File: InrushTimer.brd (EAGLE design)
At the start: 62.2 x 36 mm, 71 parts, among them IC1 TLC272D, IC2 555, IC3 4076N, Q2 TRANSISTOR-FET_2N7002, Q3 TRANSISTOR-FET_2N7002, Q4 TRANSISTOR-FET_2N7002, Q5 TRANSISTOR-FET_2N7002, Q6 DIODES_ZTX451DIODES_ZTX451_0_0, T1 MMBTA05, U1 ROHM_BY_ELEMENT14_BATCH_1_BU4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

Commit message: Layout changes.
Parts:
- moved C5 1.62 mm to (5.71, 31.4), turned to 180 degrees
- moved D4 0.32 mm to (2.06, 29.8)
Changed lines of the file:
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@@
 <setting verticaltext="up"/>
 </settings>
-<grid distance="0.05" unitdist="inch" unit="inch" style="lines" multiple="1" display="yes" altdistance="0.00625" altunitdist="inch" altunit="inch"/>
+<grid distance="0.05" unitdist="inch" unit="inch" style="lines" multiple="1" display="yes" altdistance="0.0125" altunitdist="inch" altunit="inch"/>
 <layers>
 <layer number="1" name="Top" color="4" fill="1" visible="yes" active="yes"/>
@@
 <element name="R3" library="rcl" package="0207/2V" value="10K" x="18.0975" y="9.8425" rot="R225"/>
 <element name="C10" library="rcl" package="C0805K" value="10pF (DNF)" x="73.025" y="27.305" rot="MR180"/>
-<element name="D4" library="diode" package="DO41-7.6" value="STTH110" x="2.06375" y="30.1625" rot="R270"/>
+<element name="D4" library="diode" package="DO41-7.6" value="STTH110" x="2.06375" y="29.845" rot="R270"/>
 <element name="IC1" library="linear" package="SO08" value="TLC272D" x="12.3825" y="25.4" smashed="yes" rot="MR0">
 <attribute name="NAME" x="15.0495" y="23.495" size="1.27" layer="26" rot="MR90"/>
@@
 <attribute name="MF" value="" x="56.515" y="30.7975" size="1.778" layer="27" rot="R90" display="off"/>
 </element>
-<element name="C5" library="rcl" package="C0805K" value="10nF" x="4.1275" y="31.75" rot="MR0"/>
+<element name="C5" library="rcl" package="C0805K" value="10nF" x="5.715" y="31.4325" rot="MR180"/>
 <element name="C4" library="rcl" package="C050-024X044" value="10nF" x="20.6375" y="8.255" rot="R45"/>
 <element name="C6" library="rcl" package="C0805K" value="1nF" x="18.0975" y="25.4" rot="MR90"/>
@@
 <wire x1="70.00875" y1="18.415" x2="72.920721875" y2="17.090525" width="0" layer="19" extent="1-1"/>
 <wire x1="45.24375" y1="1.74625" x2="70.00875" y2="8.255" width="0" layer="19" extent="1-1"/>
-<wire x1="41.165" y1="12.065" x2="45.24375" y2="1.74625" width="0" layer="19" extent="16-16"/>
-<wire x1="38.735" y1="9.525" x2="41.165" y2="12.065" width="0" layer="19" extent="16-16"/>
+<wire x1="38.735" y1="9.525" x2="45.24375" y2="1.74625" width="0" layer="19" extent="1-1"/>
+<wire x1="41.165" y1="12.065" x2="38.735" y2="9.525" width="0" layer="19" extent="16-16"/>
 <wire x1="32.86125" y1="16.98625" x2="38.735" y2="9.525" width="0" layer="19" extent="1-1"/>
 <wire x1="24.710525" y1="9.153025" x2="32.86125" y2="16.98625" width="0" layer="19" extent="1-1"/>
@@
 <wire x1="15.5575" y1="5.08" x2="15.5575" y2="5.395" width="0.4064" layer="16"/>
 <wire x1="17.2593" y1="3.7973" x2="17.2593" y2="5.08" width="0.4064" layer="16"/>
-<wire x1="5.1275" y1="31.75" x2="5.715" y2="31.1625" width="0.6096" layer="16"/>
-<wire x1="5.715" y1="31.1625" x2="5.715" y2="28.8925" width="0.6096" layer="16"/>
 <wire x1="5.715" y1="28.8925" x2="8.5725" y2="28.8925" width="0.6096" layer="16"/>
 <wire x1="18.995525" y1="10.740525" x2="19.25855" y2="10.4775" width="0.6096" layer="16"/>
@@
 <wire x1="10.00125" y1="22.86" x2="10.00125" y2="14.976971875" width="0.6096" layer="16"/>
 <wire x1="10.00125" y1="14.976971875" x2="10.531971875" y2="14.976971875" width="0.6096" layer="16"/>
+<wire x1="5.715" y1="28.8925" x2="5.6675" y2="28.8925" width="0.6096" layer="16"/>
+<wire x1="5.715" y1="28.8925" x2="4.715" y2="29.8925" width="0.6096" layer="16"/>
+<wire x1="4.715" y1="29.8925" x2="4.715" y2="31.4325" width="0.6096" layer="16"/>
 <wire x1="83.65" y1="32.7" x2="81.11" y2="35.24" width="0" layer="19" extent="1-1"/>
 <wire x1="77.62875" y1="26.035" x2="83.65" y2="32.7" width="0" layer="19" extent="1-1"/>
@@
 <wire x1="45.24375" y1="6.82625" x2="45.87875" y2="9.04875" width="0" layer="19" extent="1-1"/>
 <wire x1="33.765" y1="12.065" x2="42.79125" y2="14.12875" width="0" layer="19" extent="16-16"/>
+<wire x1="32.385" y1="14.605" x2="33.765" y2="12.065" width="0" layer="19" extent="16-16"/>
 <wire x1="34.501434375" y1="6.84706875" x2="33.765" y2="12.065" width="0" layer="19" extent="16-16"/>
 <wire x1="30.7975" y1="3.81" x2="34.501434375" y2="6.84706875" width="0" layer="19" extent="16-16"/>
 <wire x1="19.25855" y1="10.4775" x2="18.415" y2="5.08" width="0" layer="19" extent="16-16"/>
-<wire x1="32.385" y1="14.605" x2="33.765" y2="12.065" width="0" layer="19" extent="16-16"/>
 <wire x1="12.065" y1="11.43" x2="15.5575" y2="5.395" width="0" layer="19" extent="16-16"/>
 <wire x1="15.594253125" y1="32.42175" x2="8.73125" y2="28.73375" width="0" layer="19" extent="16-16"/>
@@
 <contactref element="IC1" pad="5"/>
 <contactref element="R8" pad="2"/>
-<wire x1="2.06375" y1="33.9725" x2="2.8575" y2="33.9725" width="0.6096" layer="16"/>
-<wire x1="2.8575" y1="33.9725" x2="5.715" y2="33.9725" width="0.6096" layer="16"/>
-<wire x1="3.1275" y1="31.75" x2="2.8575" y2="32.02" width="0.6096" layer="16"/>
-<wire x1="2.8575" y1="32.02" x2="2.8575" y2="33.9725" width="0.6096" layer="16"/>
+<wire x1="2.06375" y1="33.9725" x2="5.715" y2="33.9725" width="0.6096" layer="16"/>
 <wire x1="5.715" y1="33.9725" x2="8.255" y2="33.9725" width="0.6096" layer="16"/>
 <wire x1="8.5725" y1="31.4325" x2="8.5725" y2="33.9725" width="0.6096" layer="16"/>
@@
 <wire x1="8.89" y1="31.4325" x2="8.5725" y2="31.4325" width="0.4064" layer="16"/>
 <wire x1="10.4775" y1="28" x2="10.4775" y2="29.845" width="0.4064" layer="16"/>
+<wire x1="2.06375" y1="33.9725" x2="2.06375" y2="33.655" width="0.6096" layer="16"/>
+<wire x1="8.5725" y1="31.4325" x2="6.715" y2="31.4325" width="0.6096" layer="16"/>
 </signal>
 <signal name="N$7">
@@
 <wire x1="41.165" y1="14.605" x2="45.79125" y2="14.12875" width="0" layer="19" extent="16-16"/>
 <wire x1="41.165" y1="13.335" x2="41.165" y2="14.605" width="0" layer="19" extent="16-16"/>
-<wire x1="35.2425" y1="26.035" x2="45.79125" y2="14.12875" width="0" layer="19" extent="16-16"/>
+<wire x1="35.2425" y1="26.035" x2="41.165" y2="14.605" width="0" layer="19" extent="16-16"/>
 </signal>
 <signal name="ON_B">
@@
 <wire x1="4.425" y1="22.30375" x2="3.73125" y2="22.30375" width="1.4224" layer="16"/>
 <wire x1="3.73125" y1="22.30375" x2="2.06375" y2="23.97125" width="1.4224" layer="16"/>
-<wire x1="2.06375" y1="23.97125" x2="2.06375" y2="26.3525" width="1.4224" layer="16"/>
+<wire x1="2.06375" y1="23.97125" x2="2.06375" y2="26.035" width="1.4224" layer="16"/>
 </signal>
 <signal name="ON_A_SYNC">

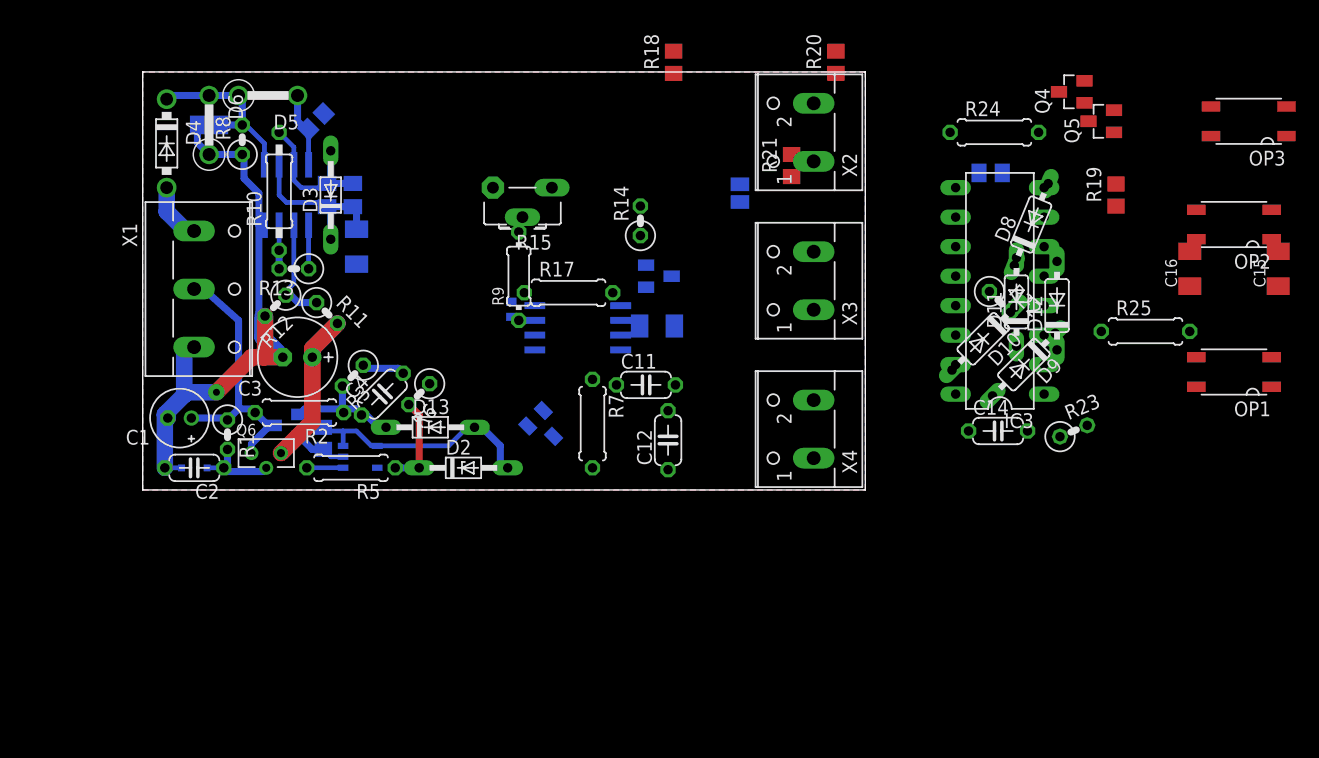
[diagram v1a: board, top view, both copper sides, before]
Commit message: ayed out the timer - starting on the D types. Fixed incorrect gate capacitance.
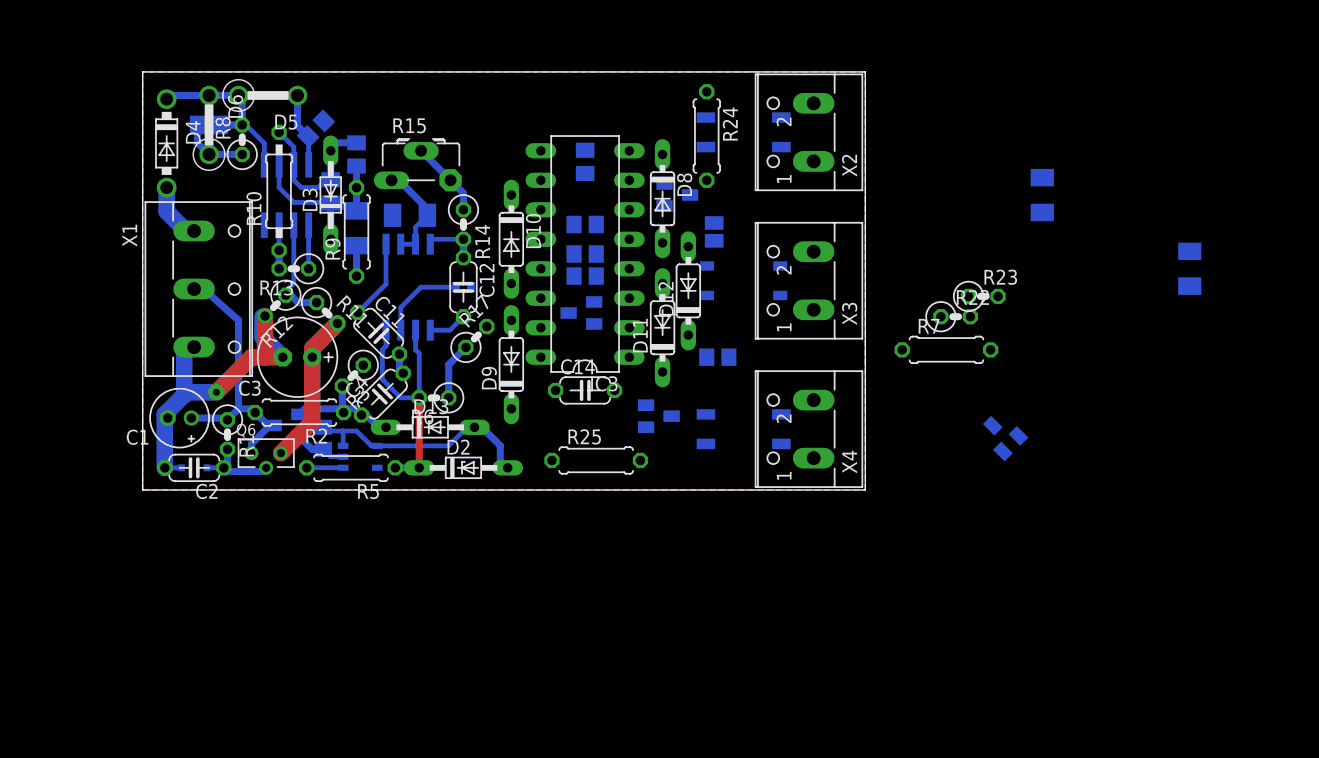
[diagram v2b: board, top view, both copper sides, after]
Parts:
- removed OP2: FODM3053, SHoleLib:FODM
- added U$1: TLP268J, SHoleLib:TLP26*
- R17: device rcl:0207/7 -> rcl:0207/2V
- R9: device rcl:0204/7 -> rcl:0207/7
- moved OP3 50.9 mm to (51.8, 5.24), flipped to the bottom
- moved R25 48.6 mm to (39.1, 2.54)
- moved OP1 47.0 mm to (51.8, 30.8), flipped to the bottom
- moved R19 46.0 mm to (38.1, 20.3), flipped to the bottom, turned to 180 degrees
- moved Q5 45.8 mm to (44.5, 6.35), flipped to the bottom
- moved D9 44.1 mm to (31.8, 10.8), turned to 90 degrees
- moved D10 41.5 mm to (31.8, 21.6), turned to 270 degrees
- moved Q2 39.4 mm to (74.0, 4.76), turned to 315 degrees
- moved IC3 35.9 mm to (38.1, 20.3)
- moved C14 35.7 mm to (38.1, 8.57)
- moved Q4 35.1 mm to (46.0, 25.4), flipped to the bottom
- moved C10 34.9 mm to (38.1, 28.3), turned to 90 degrees
- moved D8 31.8 mm to (44.8, 25.1), turned to 270 degrees
- moved D12 31.8 mm to (47.0, 17.1)
- moved R7 31.1 mm to (69.2, 12.1), turned to 0 degrees
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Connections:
- net N$17: now also U$1.2; no longer OP2.2
- net N$20: now also U$1.4; no longer OP2.4
- net N$21: now also U$1.3; no longer OP2.3
- net V12: now also U$1.1; no longer OP2.1
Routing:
- net RESET_N: track 7.89 -> 22.3 mm
- net ZERO: track 77.8 -> 66.5 mm
- net V12: track 24.3 -> 33.5 mm
- net N$28: track 0.00 -> 8.85 mm
- net N$48: track 0.00 -> 7.42 mm
- net N$40: track 0.00 -> 6.88 mm
- net N$2: track 0.00 -> 6.59 mm
- net N$9: track 15.0 -> 16.5 mm
- net N$7: track 13.2 -> 14.0 mm

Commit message: Refitted the timer and pulse generator.
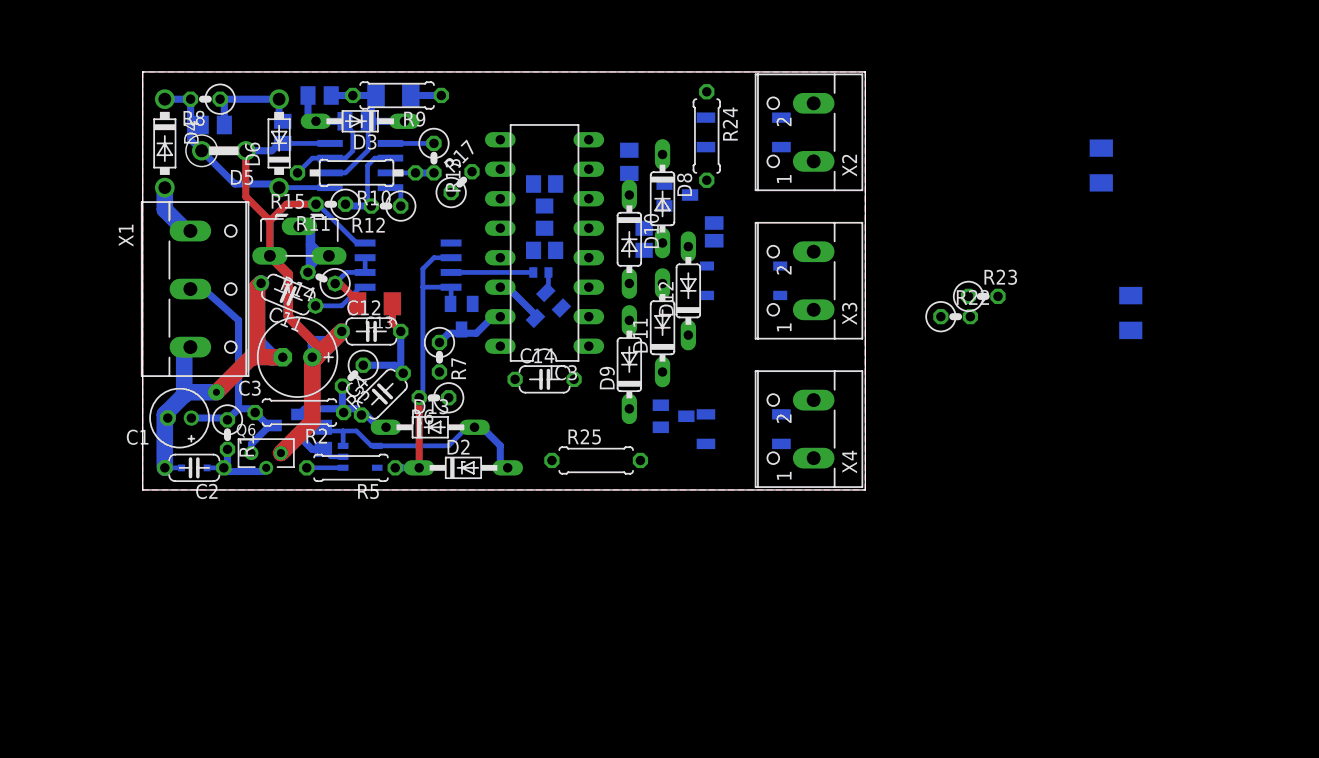
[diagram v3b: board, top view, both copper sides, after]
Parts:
- D5: device diode:DO41-10V -> diode:DO41-10VN
- D6: device diode:DO41-10V -> diode:DO41-7.6
- R15: device pot:CA6H_MOD -> pot:CA6H
- R7: device rcl:0207/7 -> rcl:0207/2V
- moved Q2 47.6 mm to (27.5, 14.9), turned to 180 degrees
- moved R7 43.7 mm to (25.6, 11.4), turned to 270 degrees
- moved R13 15.4 mm to (25.1, 28.6), turned to 270 degrees
- moved R17 13.4 mm to (27.5, 26.5)
- moved R14 13.1 mm to (15.4, 18.3), turned to 157.5 degrees
- moved R12 12.8 mm to (21.0, 24.4), turned to 180 degrees
- moved R15 12.3 mm to (13.5, 20.2)
- moved R9 12.3 mm to (21.9, 34.0), turned to 180 degrees
- moved R21 12.0 mm to (43.2, 21.6), turned to 90 degrees
- moved C9 11.9 mm to (21.6, 34.0), turned to 180 degrees
- moved D10 10.2 mm to (41.9, 21.6)
- moved D9 10.2 mm to (41.9, 10.8)
- moved R11 9.37 mm to (16.2, 24.6), turned to 180 degrees
- moved C12 8.80 mm to (19.7, 13.7), turned to 0 degrees
- moved C11 8.46 mm to (12.5, 16.8), turned to 157.5 degrees
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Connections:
- net N$2: now also R14.2; no longer R14.1
- net N$28: now also R14.1; no longer R15.A
- net RESET: now also R7.1; no longer R7.2
- net THRESH: now also R12.2; no longer R12.1
- net V12: now also R15.A, R7.2; no longer R14.2, R7.1
- net ZERO: now also R12.1; no longer R12.2
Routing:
- net V12: track 33.5 -> 75.2 mm
- net ZERO: track 66.5 -> 83.8 mm
- net RESET: track 0.00 -> 6.16 mm
- net N$11: track 15.6 -> 20.7 mm
- net ON_B: track 0.00 -> 4.31 mm
- net RESET_N: track 22.3 -> 26.2 mm
- net N$40: track 6.88 -> 4.94 mm
- net N$36: track 0.00 -> 1.82 mm
- net N$2: track 6.59 -> 8.40 mm
- net N$28: track 8.85 -> 7.11 mm
- net THRESH: track 9.22 -> 8.14 mm

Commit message: Everything on the board - not routed.
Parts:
- moved C16 44.7 mm to (40.6, 10.2), turned to 315 degrees
- moved C15 39.9 mm to (42.9, 32.4), turned to 0 degrees
- moved R23 31.4 mm to (44.5, 2.38), turned to 180 degrees
- moved R22 20.9 mm to (49.7, 9.84)
- moved C10 8.03 mm to (34.3, 30.8)
- moved R25 2.84 mm to (36.5, 3.81)
- moved R21 1.27 mm to (41.9, 21.6)
- moved Q5 0.63 mm to (45.1, 6.35)

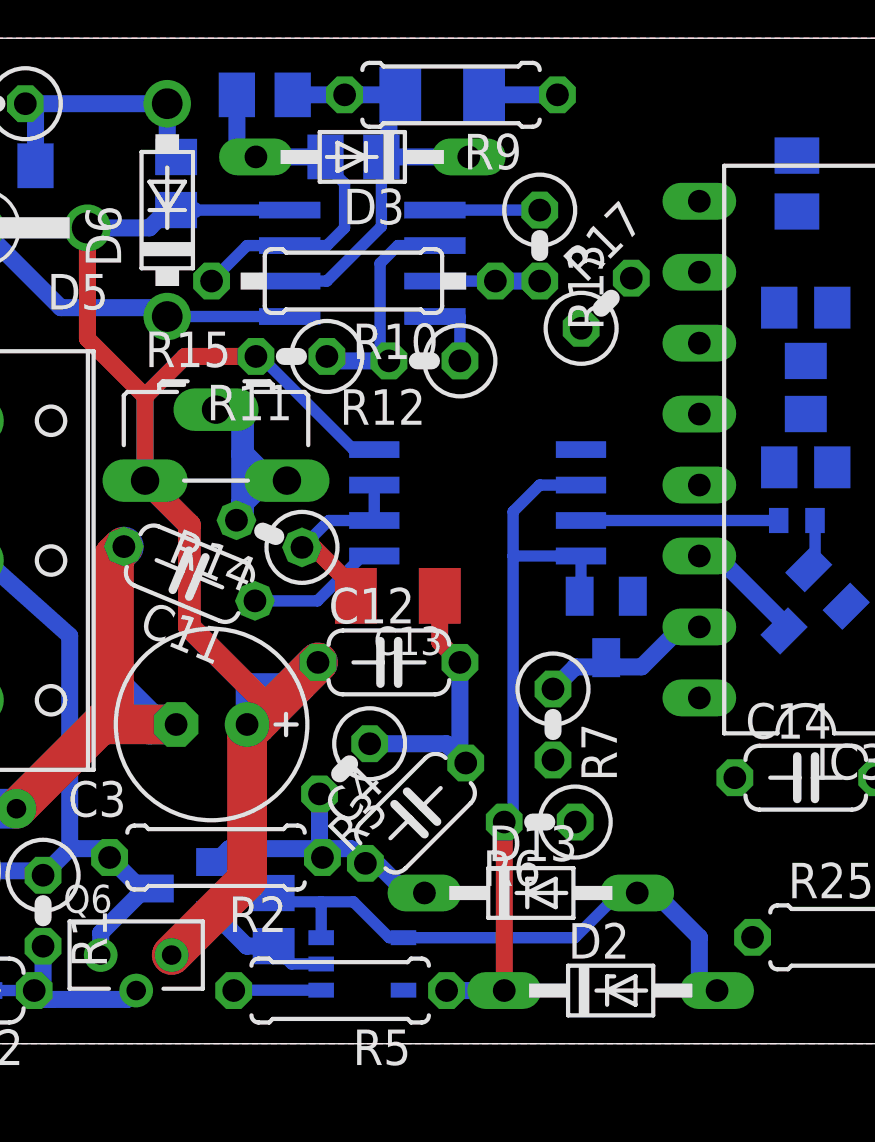
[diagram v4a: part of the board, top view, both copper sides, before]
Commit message: Added a couple more power routes.
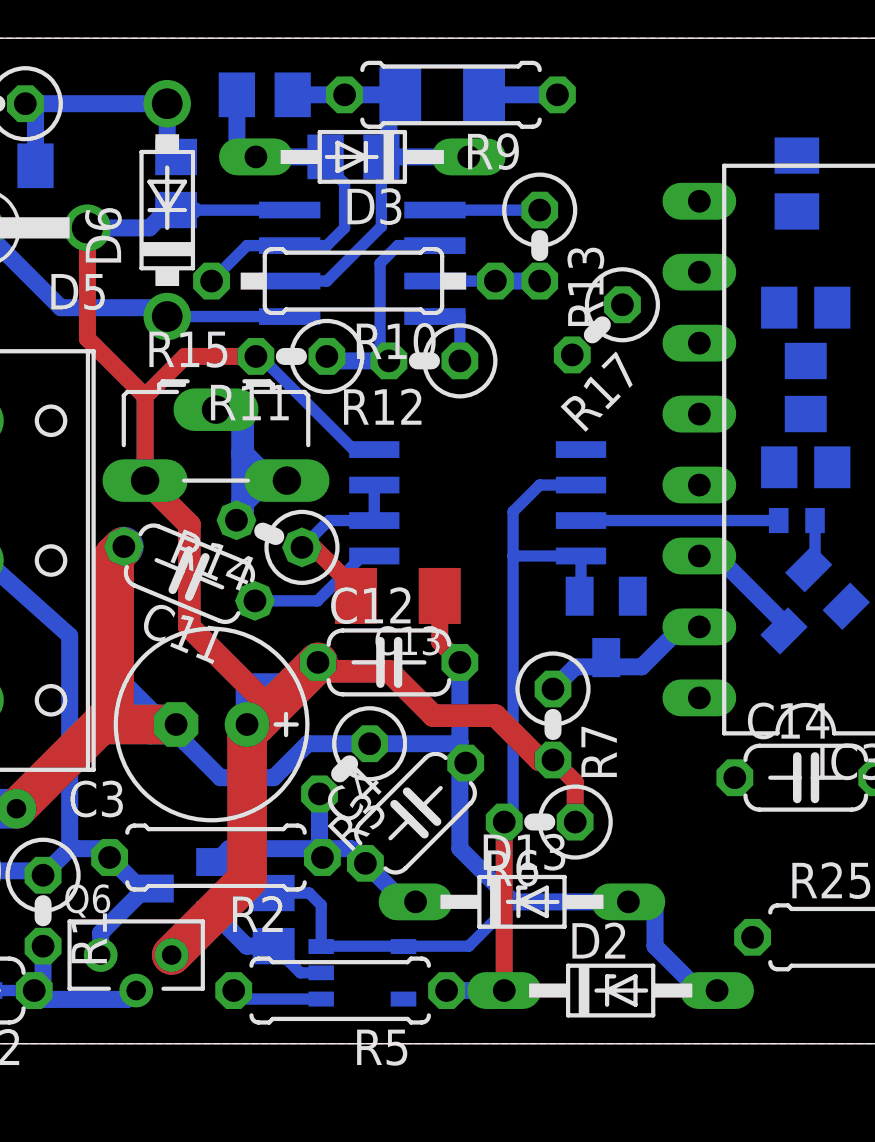
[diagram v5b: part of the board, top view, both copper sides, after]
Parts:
- moved R17 1.00 mm to (27.1, 25.6), turned to 225 degrees
- moved D13 0.45 mm to (24.4, 5.08)
- moved U1 0.32 mm to (18.7, 2.54)
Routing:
- net ZERO: track 83.8 -> 97.2 mm
- net V12: track 75.2 -> 87.6 mm
